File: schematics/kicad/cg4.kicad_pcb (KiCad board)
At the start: 4 copper layers, 228 x 195.5 mm, 139 parts, among them J7 DE15_Socket_HighDensity, K1300 10uF, P4 DIN41612_03x32_C_Split, U1000 PAL16R8, U1001 PAL20X10, U1002 PAL20X10, U1003 PAL20X10, U1004 PAL20R6, U1005 P16L8, U1006 PAL16R8, U1007 P20L8, U1008 P16L8, U1009 P16L8, U1010 P16L8, U1015 74F175, U1016 74F244, U1017 330Ω, U1021 330Ω, U1036 330Ω, U1037 330Ω, U1038 330Ω, U1100 74F257, U1101 74F257, U1102 74F257, U1103 74F257, U1104 330Ω, U1105 330Ω, U1110 74F257, U1111 74F257, U1112 74F257, U1113 74F257, U1114 330Ω, U1129 74LS393, U1200 HM53461, U1201 HM53461, U1202 HM53461, U1203 HM53461, U1204 HM53461, U1205 HM53461, U1206 HM53461, U1207 HM53461, U1208 HM53461, U1209 HM53461, U1210 HM53461, U1211 HM53461, U1212 HM53461, U1213 HM53461, U1214 HM53461, U1215 HM53461, U1216 HM53461, U1217 HM53461, U1218 HM53461, U1219 HM53461, U1220 HM53461, U1221 HM53461, U1222 HM53461, U1223 HM53461, U1224 HM53461, U1225 HM53461, U1226 HM53461, U1227 HM53461, U1228 HM53461, U1229 HM53461, U1230 HM53461, U1231 HM53461, U1300 HM53461, U1301 HM53461, U1302 HM53461, U1303 HM53461, U1304 HM53461, U1305 HM53461, U1306 HM53461, U1307 HM53461, U1310 BT458, U1311 92.9405Mhz, U1312 10H101, U1313 10H131, U1314 10H350, U1315 LM385BZ-1.2, U1318 74F08

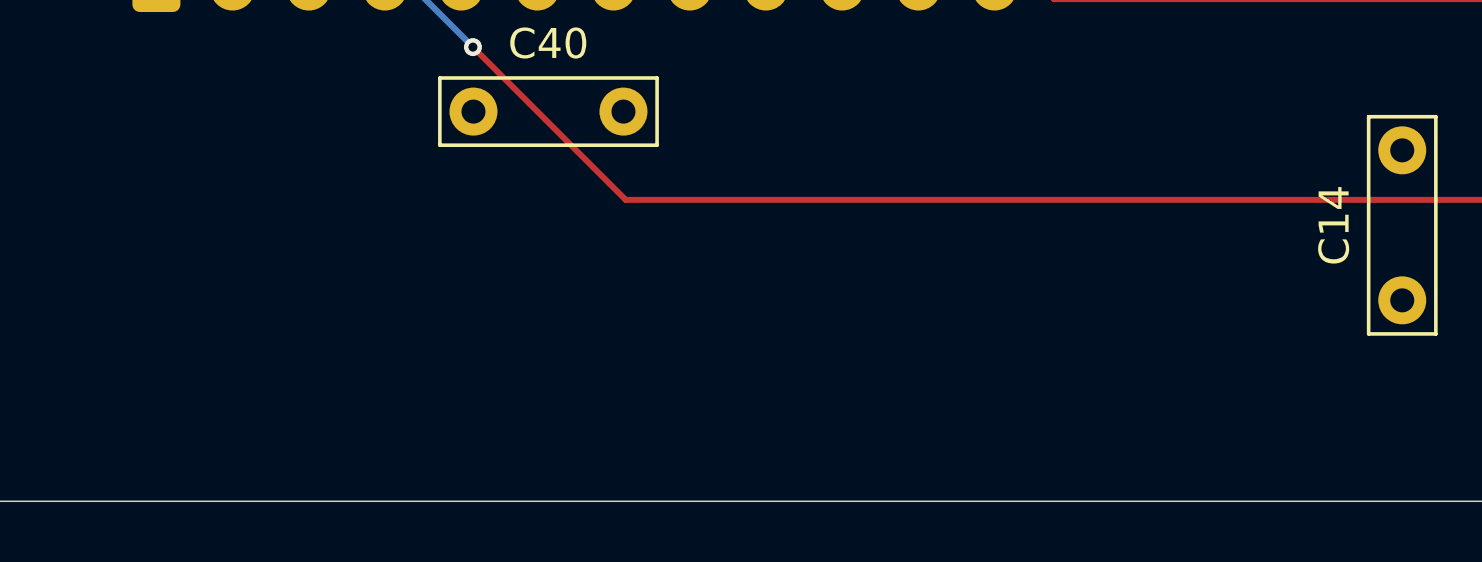
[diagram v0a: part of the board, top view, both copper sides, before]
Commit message: Add back reference silkscreen, name the board
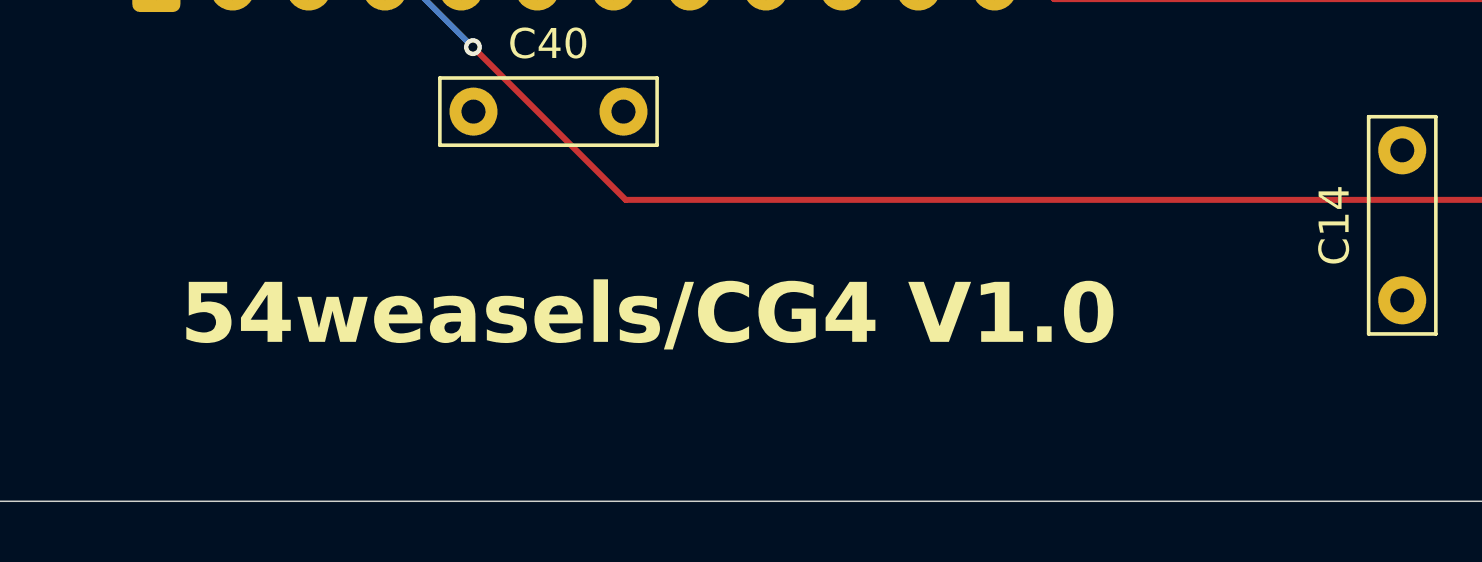
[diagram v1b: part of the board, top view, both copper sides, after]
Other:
- board text added: "54weasels/CG4 V1.0"
